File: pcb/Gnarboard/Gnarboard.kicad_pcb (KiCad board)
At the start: 2 copper layers, 157.5 x 124.5 mm, 108 parts, among them J1 Screw_Terminal_01x08, J2 Screw_Terminal_01x08, J3 Screw_Terminal_01x12, J4 Screw_Terminal_01x12, Q1 MMBT5551L, Q10 IRF4905, Q11 MMBT5551L, Q12 IRF4905, Q13 MMBT5551L, Q14 IRF4905, Q15 MMBT5551L, Q16 IRF4905, Q2 IRF4905, Q3 MMBT5551L, Q4 IRF4905, Q5 MMBT5551L, Q6 IRF4905, Q7 MMBT5551L, Q8 IRF4905, Q9 MMBT5551L, U10 ACS725xLCTR-20AU, U11 ACS725xLCTR-20AU, U12 ACS725xLCTR-20AU, U2 MCP3208, U4 D24V5F3, U5 ACS725xLCTR-20AU, U6 ACS725xLCTR-20AU, U7 ACS725xLCTR-20AU, U8 ACS725xLCTR-20AU, U9 ACS725xLCTR-20AU

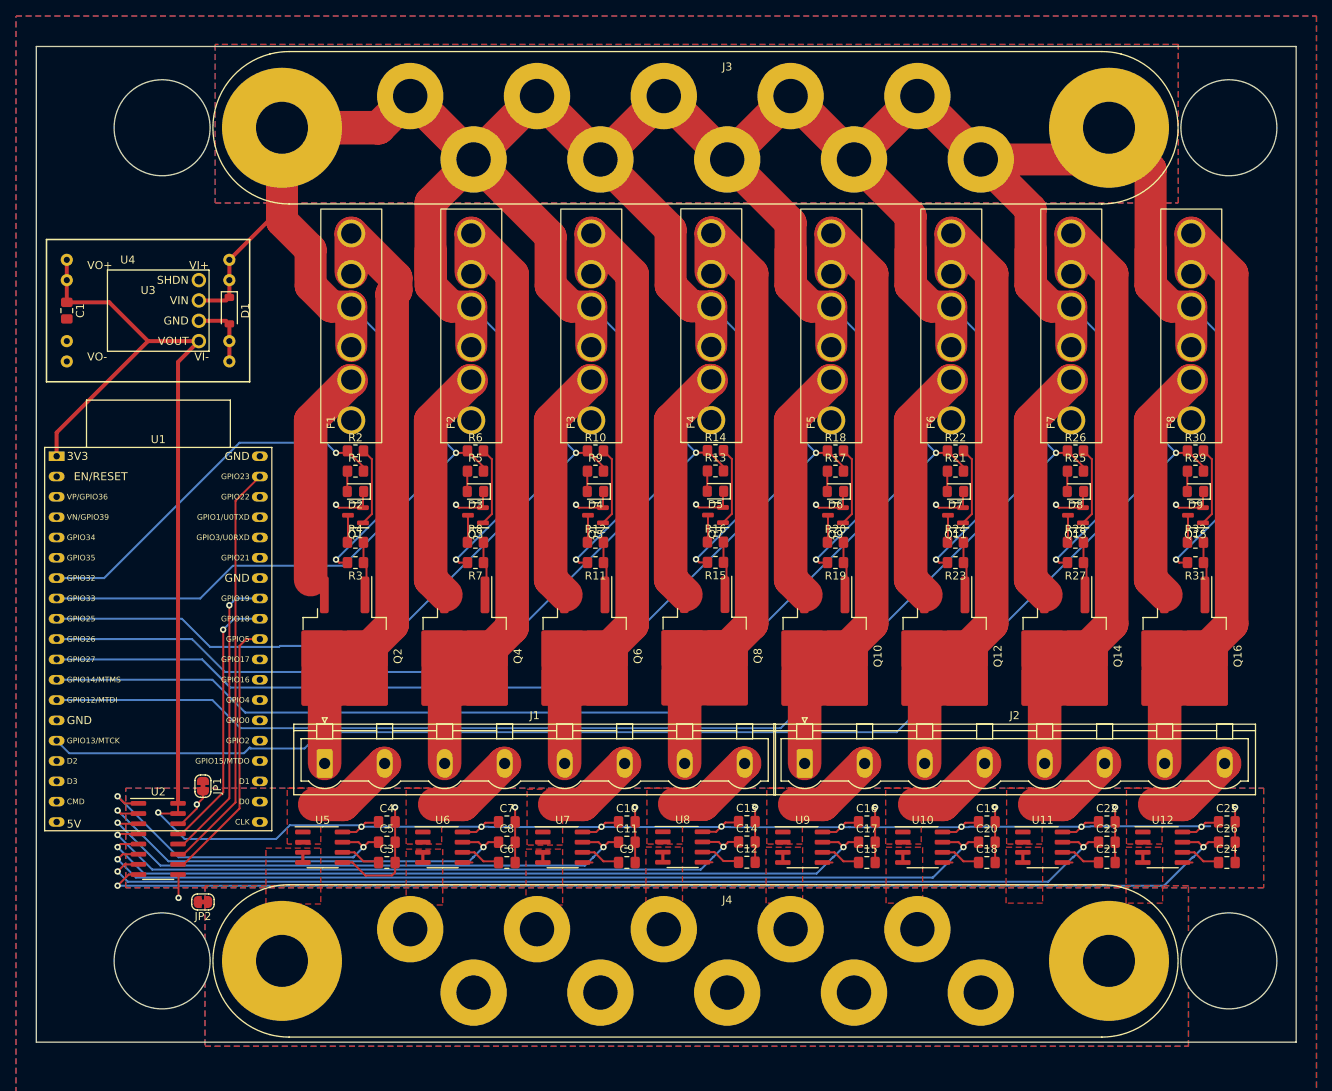
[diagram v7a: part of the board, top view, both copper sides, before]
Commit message: board close to being ready for a prototype
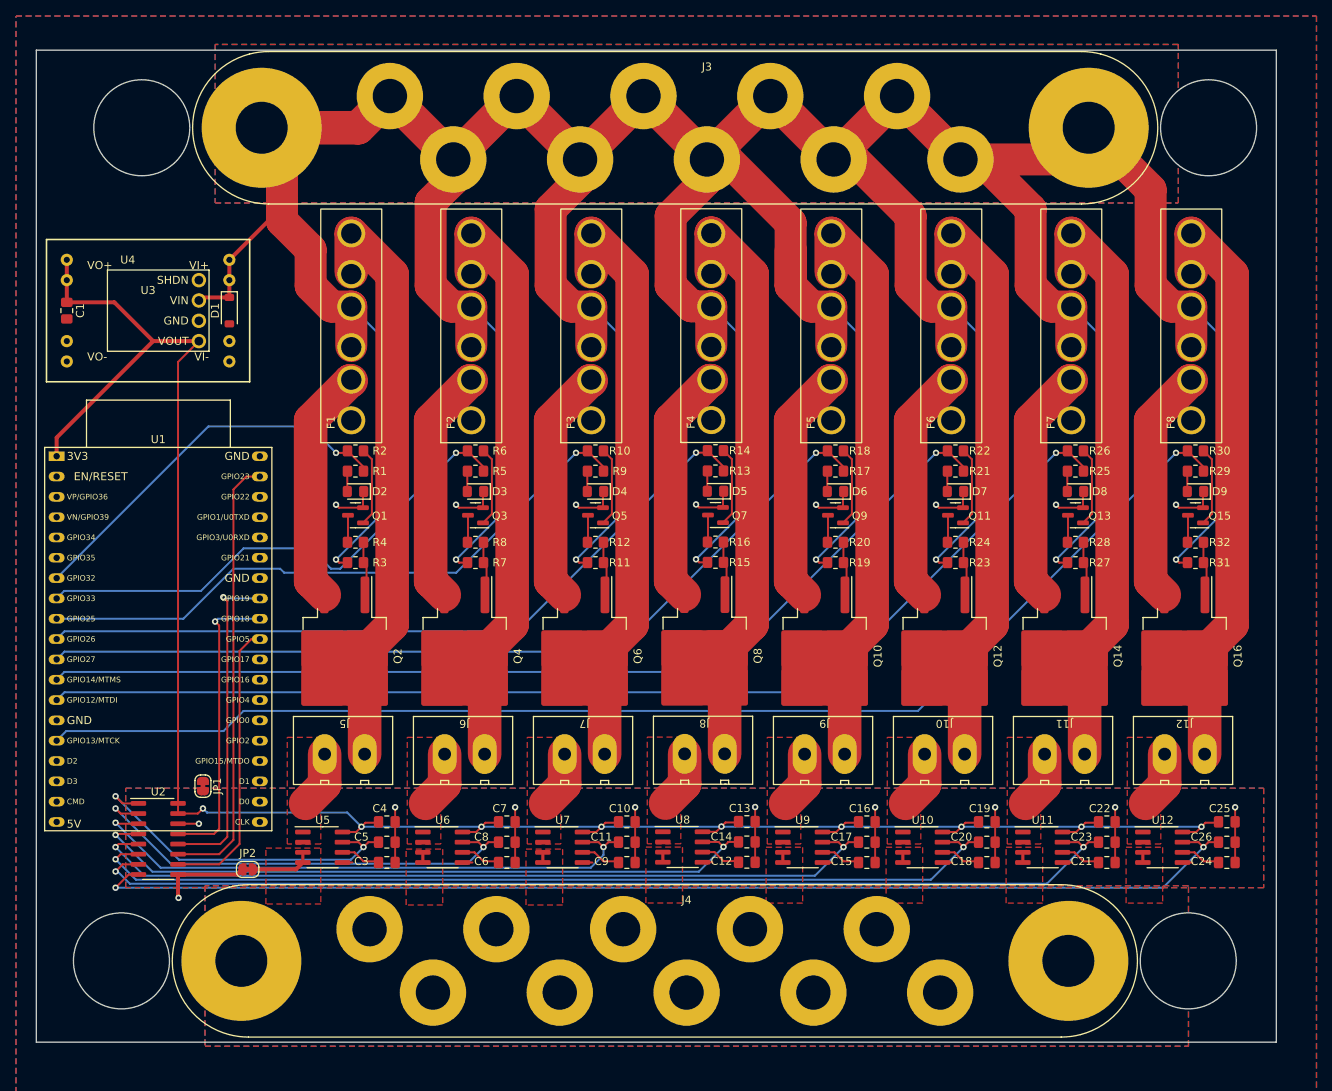
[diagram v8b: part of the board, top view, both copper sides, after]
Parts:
- removed J1, J2: Screw_Terminal_01x08, Connector_Phoenix_GMSTB:PhoenixContact_GMSTBVA_2,5_8-G_1x08_P7.50mm_Vertical
- added J10: Screw_Terminal_01x02, gnarboard:Amphenol OQ02715, F.Cu at (174.5, 117.7)
- added J11: Screw_Terminal_01x02, gnarboard:Amphenol OQ02715, F.Cu at (189.5, 117.7)
- added J12: Screw_Terminal_01x02, gnarboard:Amphenol OQ02715, F.Cu at (204.5, 117.7)
- added J5: Screw_Terminal_01x02, gnarboard:Amphenol OQ02715, F.Cu at (99.5, 117.7)
- added J6: Screw_Terminal_01x02, gnarboard:Amphenol OQ02715, F.Cu at (114.5, 117.7)
- added J7: Screw_Terminal_01x02, gnarboard:Amphenol OQ02715, F.Cu at (129.5, 117.7)
- added J8: Screw_Terminal_01x02, gnarboard:Amphenol OQ02715, F.Cu at (144.5, 117.6)
- added J9: Screw_Terminal_01x02, gnarboard:Amphenol OQ02715, F.Cu at (159.5, 117.7)
- moved JP2 6.91 mm to (87.4, 132.1)
- moved J4 5.08 mm to (142.2, 143.5)
- moved J3 2.54 mm to (144.8, 39.4)
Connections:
- net /CH+0 renamed Net-(J5-Pin_1)
- net /CH+1 renamed Net-(J6-Pin_1)
- net /CH+2 renamed Net-(J7-Pin_1)
- net /CH+3 renamed Net-(J8-Pin_1)
- net /CH+4 renamed Net-(J9-Pin_1)
- net /CH+5 renamed Net-(J10-Pin_1)
- net /CH+6 renamed Net-(J11-Pin_1)
- net /CH+7 renamed Net-(J12-Pin_1)
- net /CH-0 renamed Net-(J5-Pin_2)
- net /CH-1 renamed Net-(J6-Pin_2)
- net /CH-2 renamed Net-(J7-Pin_2)
- net /CH-3 renamed Net-(J8-Pin_2)
- net /CH-4 renamed Net-(J9-Pin_2)
- net /CH-5 renamed Net-(J10-Pin_2)
- net /CH-6 renamed Net-(J11-Pin_2)
- net /CH-7 renamed Net-(J12-Pin_2)
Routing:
- net +24V: track 719.0 -> 706.2 mm
- net GNDA: track 79.4 -> 69.0 mm
- net +3.3V: track 280.2 -> 271.5 mm
- net GNDPWR: track 10.2 -> 16.8 mm
- net /PWM3: track 99.1 -> 93.9 mm
- net /PWM5: track 131.2 -> 126.0 mm
- net /PWM4: track 114.7 -> 110.0 mm
- net /PWM6: track 146.8 -> 142.1 mm
- net /PWM2: track 82.6 -> 78.3 mm
- net Net-(U1-GPIO19): track 37.1 -> 41.4 mm
- net Net-(U1-GPIO18): track 33.3 -> 37.3 mm
- net Net-(J5-Pin_1): track 75.8 -> 71.9 mm
- net Net-(J6-Pin_2): track 10.9 -> 7.15 mm
- net Net-(J5-Pin_2): track 10.9 -> 7.15 mm
- net Net-(J7-Pin_2): track 10.9 -> 7.15 mm
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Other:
- board size 157.5 x 124.5 mm -> 155 x 124 mm
